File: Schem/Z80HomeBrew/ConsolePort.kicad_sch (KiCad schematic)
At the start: 12 parts, among them J3 0480370001, U14 FT230XS

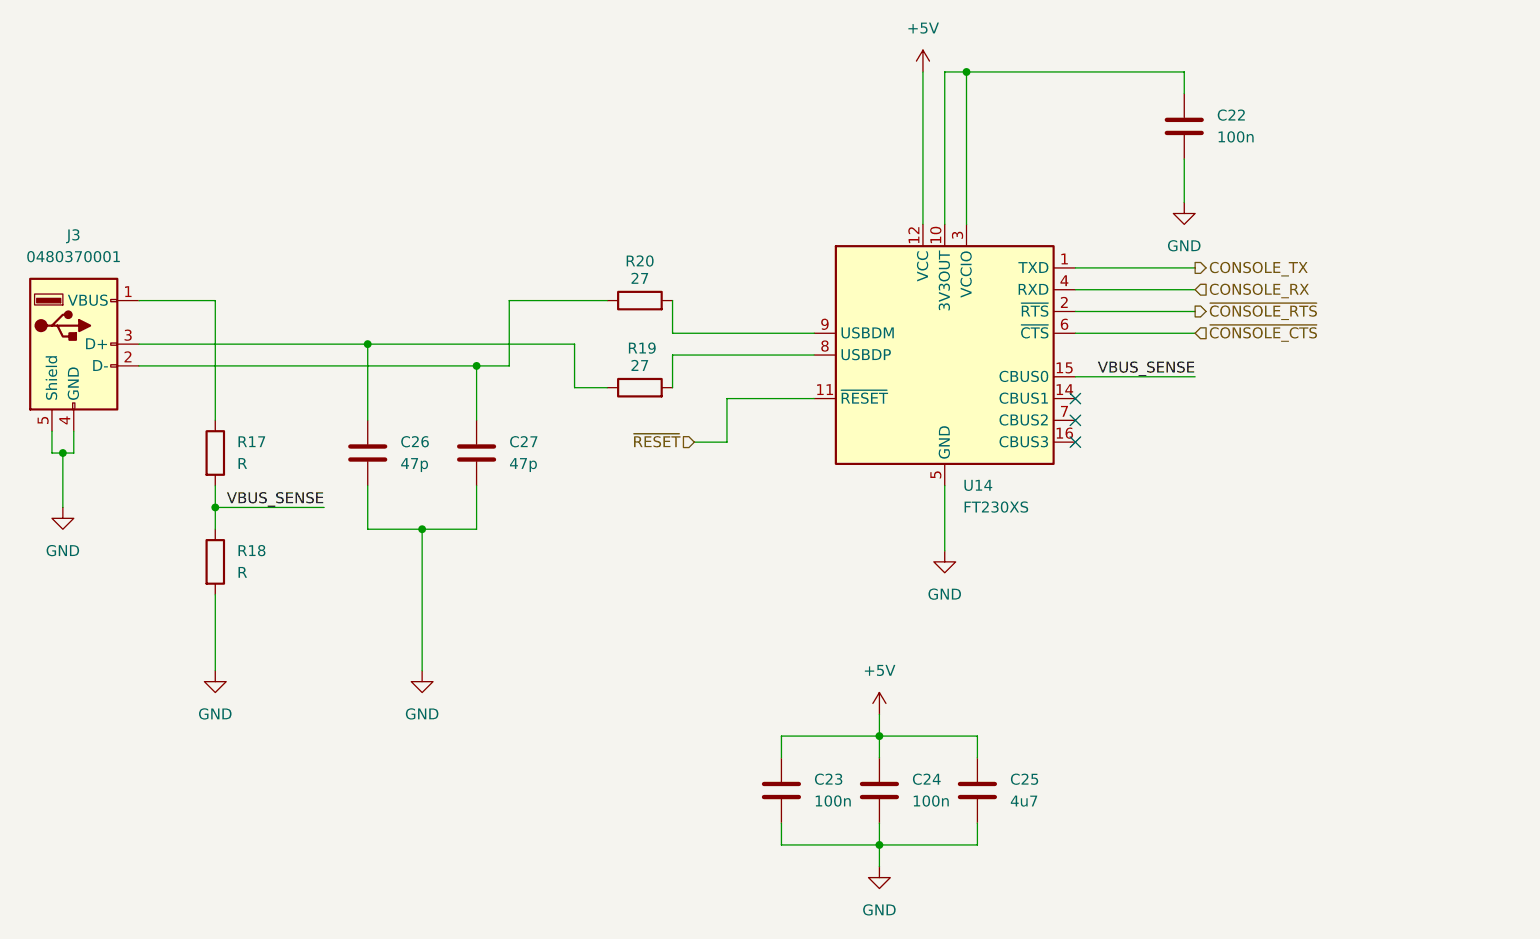
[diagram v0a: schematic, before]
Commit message: Video block added. fixed some issues with parts...
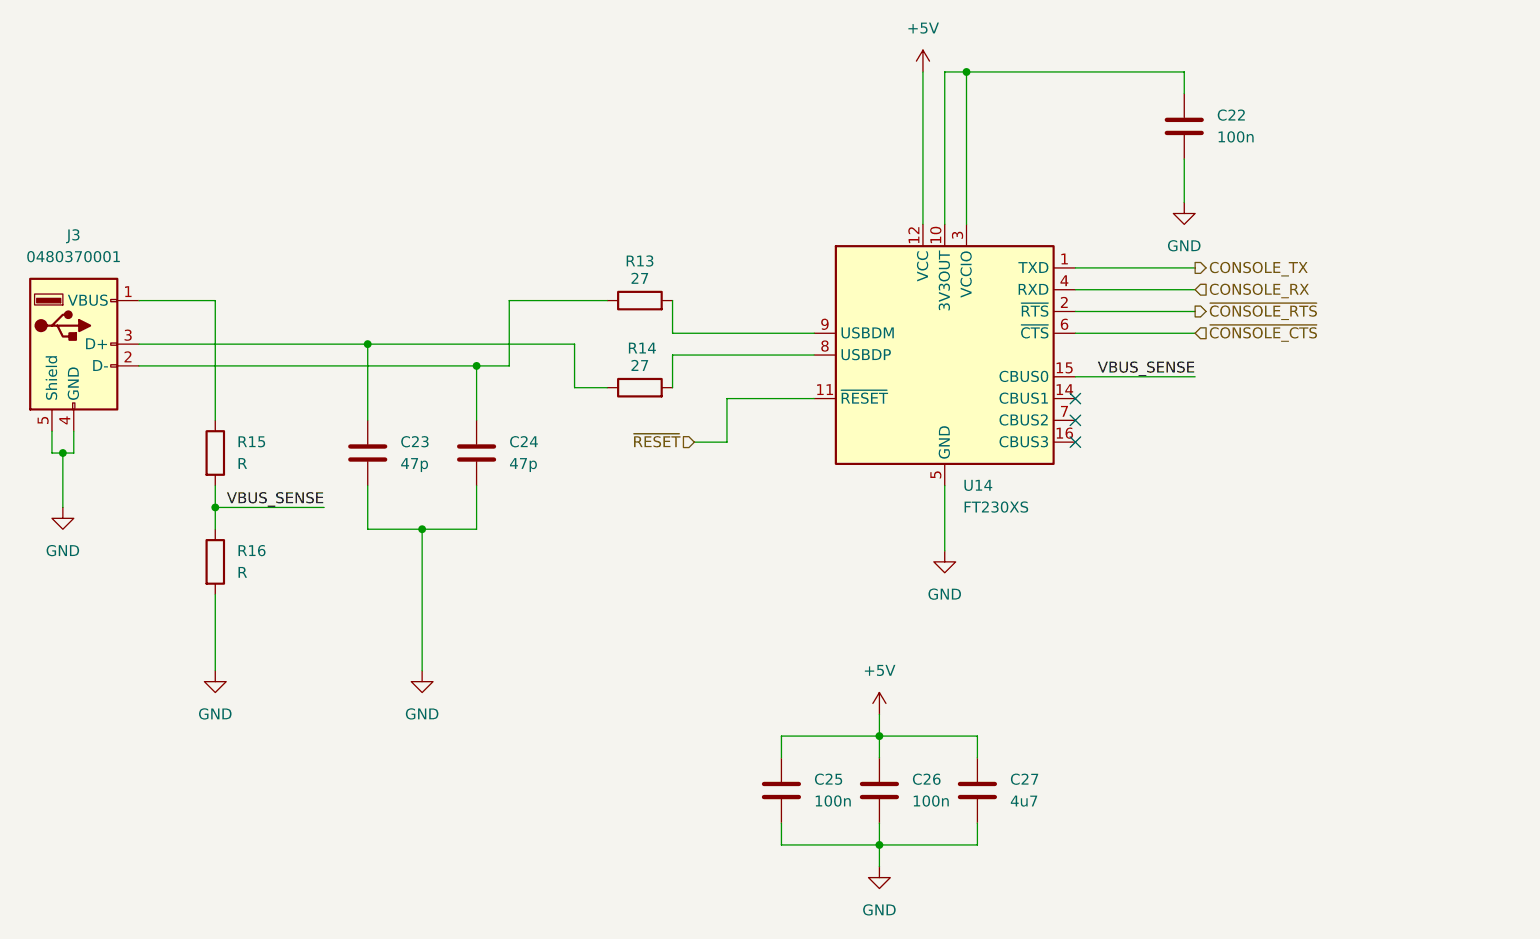
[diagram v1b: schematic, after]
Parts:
- renumbered C26 to C23, C27 to C24, C23 to C25, C24 to C26, C25 to C27, R20 to R13, R19 to R14, R17 to R15, R18 to R16
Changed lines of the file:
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@@
 		(dnp no)
 		(fields_autoplaced yes)
-		(property "Reference" "#PWR050"
+		(property "Reference" "#PWR054"
 			(at 153.67 38.1 0)
 			(effects
@@
 			(project ""
 				(path "/5593e793-d133-45d0-a91e-72805049e474/685e3ad0-b668-4082-bf36-08a728699034"
-					(reference "#PWR050")
+					(reference "#PWR054")
 					(unit 1)
 				)
@@
 		(dnp no)
 		(fields_autoplaced yes)
-		(property "Reference" "#PWR048"
+		(property "Reference" "#PWR055"
 			(at 184.15 55.88 0)
 			(effects
@@
 			(project ""
 				(path "/5593e793-d133-45d0-a91e-72805049e474/685e3ad0-b668-4082-bf36-08a728699034"
-					(reference "#PWR048")
+					(reference "#PWR055")
 					(unit 1)
 				)
@@
 		(dnp no)
 		(fields_autoplaced yes)
-		(property "Reference" "C24"
+		(property "Reference" "C26"
 			(at 152.4 116.8399 0)
 			(effects
@@
 			(project "Z80HomeBrew"
 				(path "/5593e793-d133-45d0-a91e-72805049e474/685e3ad0-b668-4082-bf36-08a728699034"
-					(reference "C24")
+					(reference "C26")
 					(unit 1)
 				)
@@
 		(on_board yes)
 		(dnp no)
-		(property "Reference" "R19"
+		(property "Reference" "R14"
 			(at 120.904 66.548 90)
 			(effects
@@
 			(project "Z80HomeBrew"
 				(path "/5593e793-d133-45d0-a91e-72805049e474/685e3ad0-b668-4082-bf36-08a728699034"
-					(reference "R19")
+					(reference "R14")
 					(unit 1)
 				)
@@
 		(on_board yes)
 		(dnp no)
-		(property "Reference" "R20"
+		(property "Reference" "R13"
 			(at 120.65 56.388 90)
 			(effects
@@
 			(project "Z80HomeBrew"
 				(path "/5593e793-d133-45d0-a91e-72805049e474/685e3ad0-b668-4082-bf36-08a728699034"
-					(reference "R20")
+					(reference "R13")
 					(unit 1)
 				)
@@
 		(dnp no)
 		(fields_autoplaced yes)
-		(property "Reference" "#PWR051"
+		(property "Reference" "#PWR060"
 			(at 148.59 113.03 0)
 			(effects
@@
 			(project "Z80HomeBrew"
 				(path "/5593e793-d133-45d0-a91e-72805049e474/685e3ad0-b668-4082-bf36-08a728699034"
-					(reference "#PWR051")
+					(reference "#PWR060")
 					(unit 1)
 				)
@@
 		(dnp no)
 		(fields_autoplaced yes)
-		(property "Reference" "#PWR049"
+		(property "Reference" "#PWR057"
 			(at 156.21 96.52 0)
 			(effects
@@
 			(project "Z80HomeBrew"
 				(path "/5593e793-d133-45d0-a91e-72805049e474/685e3ad0-b668-4082-bf36-08a728699034"
-					(reference "#PWR049")
+					(reference "#PWR057")
 					(unit 1)
 				)
@@
 		(dnp no)
 		(fields_autoplaced yes)
-		(property "Reference" "#PWR052"
+		(property "Reference" "#PWR061"
 			(at 148.59 133.35 0)
 			(effects
@@
 			(project "Z80HomeBrew"
 				(path "/5593e793-d133-45d0-a91e-72805049e474/685e3ad0-b668-4082-bf36-08a728699034"
-					(reference "#PWR052")
+					(reference "#PWR061")
 					(unit 1)
 				)
@@
 		(dnp no)
 		(fields_autoplaced yes)
-		(property "Reference" "C25"
+		(property "Reference" "C27"
 			(at 163.83 116.8399 0)
 			(effects
@@
 			(project "Z80HomeBrew"
 				(path "/5593e793-d133-45d0-a91e-72805049e474/685e3ad0-b668-4082-bf36-08a728699034"
-					(reference "C25")
+					(reference "C27")
 					(unit 1)
 				)
@@
 		(dnp no)
 		(fields_autoplaced yes)
-		(property "Reference" "C23"
+		(property "Reference" "C25"
 			(at 140.97 116.8399 0)
 			(effects
@@
 			(project "Z80HomeBrew"
 				(path "/5593e793-d133-45d0-a91e-72805049e474/685e3ad0-b668-4082-bf36-08a728699034"
-					(reference "C23")
+					(reference "C25")
 					(unit 1)
 				)
@@
 		(dnp no)
 		(fields_autoplaced yes)
-		(property "Reference" "R17"
+		(property "Reference" "R15"
 			(at 73.66 77.4699 0)
 			(effects
@@
 			(project ""
 				(path "/5593e793-d133-45d0-a91e-72805049e474/685e3ad0-b668-4082-bf36-08a728699034"
-					(reference "R17")
+					(reference "R15")
 					(unit 1)
 				)
@@
 		(dnp no)
 		(fields_autoplaced yes)
-		(property "Reference" "C26"
+		(property "Reference" "C23"
 			(at 92.71 77.4699 0)
 			(effects
@@
 			(project "Z80HomeBrew"
 				(path "/5593e793-d133-45d0-a91e-72805049e474/685e3ad0-b668-4082-bf36-08a728699034"
-					(reference "C26")
+					(reference "C23")
 					(unit 1)
 				)
@@
 		(dnp no)
 		(fields_autoplaced yes)
-		(property "Reference" "C27"
+		(property "Reference" "C24"
 			(at 105.41 77.4699 0)
 			(effects
@@
 			(project "Z80HomeBrew"
 				(path "/5593e793-d133-45d0-a91e-72805049e474/685e3ad0-b668-4082-bf36-08a728699034"
-					(reference "C27")
+					(reference "C24")
 					(unit 1)
 				)
@@
 		(dnp no)
 		(fields_autoplaced yes)
-		(property "Reference" "#PWR054"
+		(property "Reference" "#PWR059"
 			(at 95.25 110.49 0)
 			(effects
@@
 			(project "Z80HomeBrew"
 				(path "/5593e793-d133-45d0-a91e-72805049e474/685e3ad0-b668-4082-bf36-08a728699034"
-					(reference "#PWR054")
+					(reference "#PWR059")
 					(unit 1)
 				)
@@
 		(dnp no)
 		(fields_autoplaced yes)
-		(property "Reference" "#PWR055"
+		(property "Reference" "#PWR056"
 			(at 53.34 91.44 0)
 			(effects
@@
 			(project "Z80HomeBrew"
 				(path "/5593e793-d133-45d0-a91e-72805049e474/685e3ad0-b668-4082-bf36-08a728699034"
-					(reference "#PWR055")
+					(reference "#PWR056")
 					(unit 1)
 				)
@@
 		(dnp no)
 		(fields_autoplaced yes)
-		(property "Reference" "#PWR053"
+		(property "Reference" "#PWR058"
 			(at 71.12 110.49 0)
 			(effects
@@
 			(project "Z80HomeBrew"
 				(path "/5593e793-d133-45d0-a91e-72805049e474/685e3ad0-b668-4082-bf36-08a728699034"
-					(reference "#PWR053")
+					(reference "#PWR058")
 					(unit 1)
 				)
@@
 		(dnp no)
 		(fields_autoplaced yes)
-		(property "Reference" "R18"
+		(property "Reference" "R16"
 			(at 73.66 90.1699 0)
 			(effects
@@
 			(project "Z80HomeBrew"
 				(path "/5593e793-d133-45d0-a91e-72805049e474/685e3ad0-b668-4082-bf36-08a728699034"
-					(reference "R18")
-					(unit 1)
-				)
+					(reference "R16")
+					(unit 1)
+				)

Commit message: Completed schematics
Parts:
- U14: value FT230XS -> FT230XS-U
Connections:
- net VBUS_SENSE: no longer U14.15 (CBUS0)
- net ~{CONSOLE_CTS} renamed CONSOLE_CTS
- net ~{CONSOLE_RTS} renamed CONSOLE_RTS
- new net CONSOLE_DTR: U14.15 (CBUS0)
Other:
- note added: "Configure the FT230 so that CBUS0 (PWREN#) is asserted (low) to signal that a terminal is connected (DTR)"
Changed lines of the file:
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@@
 	(generator_version "9.0")
 	(paper "USLedger")
+	(text "Configure the FT230 so that \nCBUS0 (PWREN#) is asserted \n(low) to signal that a terminal\nis connected (DTR)"
+		(exclude_from_sim no)
+		(at 173.482 75.438 0)
+		(effects
+			(font
+				(size 1.27 1.27)
+			)
+			(justify left)
+		)
+	)
 	(junction
 		(at 148.59 124.46)
@@
 		(color 0 0 0 0)
 	)
+	(junction
+		(at 67.31 60.96)
+		(diameter 0)
+		(color 0 0 0 0)
+	)
 	(no_connect
 		(at 171.45 72.39)
@@
 	(wire
 		(pts
-			(xy 62.23 60.96) (xy 71.12 60.96)
+			(xy 62.23 60.96) (xy 67.31 60.96)
 		)
 		(stroke
@@
 		(pts
 			(xy 124.46 71.12) (xy 124.46 67.31)
+		)
+		(stroke
+			(width 0)
+			(type default)
+		)
+	)
+	(wire
+		(pts
+			(xy 67.31 60.96) (xy 71.12 60.96)
 		)
 		(stroke
@@
 		)
 	)
-	(label "VBUS_SENSE"
-		(at 185.42 69.85 180)
+	(hierarchical_label "CONSOLE_RTS"
+		(shape output)
+		(at 185.42 62.23 0)
 		(effects
 			(font
 				(size 1.27 1.27)
 			)
-			(justify right bottom)
-		)
-	)
-	(hierarchical_label "~{CONSOLE_RTS}"
+			(justify left)
+		)
+	)
+	(hierarchical_label "CONSOLE_DTR"
 		(shape output)
-		(at 185.42 62.23 0)
+		(at 185.42 69.85 0)
 		(effects
 			(font
@@
 		)
 	)
-	(hierarchical_label "~{CONSOLE_CTS}"
+	(hierarchical_label "CONSOLE_CTS"
 		(shape input)
 		(at 185.42 64.77 0)
@@
 			)
 		)
-		(property "Value" "FT230XS"
+		(property "Value" "FT230XS-U"
 			(at 158.3533 85.09 0)
 			(effects
@@
 					(unit 1)
 				)
+			)
+		)
+	)
+	(symbol
+		(lib_id "power:PWR_FLAG")
+		(at 67.31 60.96 0)
+		(unit 1)
+		(exclude_from_sim no)
+		(in_bom yes)
+		(on_board yes)
+		(dnp no)
+		(fields_autoplaced yes)
+		(property "Reference" "#FLG05"
+			(at 67.31 59.055 0)
+			(effects
+				(font
+					(size 1.27 1.27)
+				)
+				(hide yes)
+			)
+		)
+		(property "Value" "PWR_FLAG"
+			(at 67.31 55.88 0)
+			(effects
+				(font
+					(size 1.27 1.27)
+				)
+			)
+		)
+		(property "Footprint" ""
+			(at 67.31 60.96 0)
+			(effects
+				(font
+					(size 1.27 1.27)
+				)
+				(hide yes)
+			)
+		)
+		(property "Datasheet" "~"
+			(at 67.31 60.96 0)
+			(effects
+				(font
+					(size 1.27 1.27)
+				)
+				(hide yes)
+			)
+		)
+		(property "Description" "Special symbol for telling ERC where power comes from"
+			(at 67.31 60.96 0)
+			(effects
+				(font
+					(size 1.27 1.27)
+				)
+				(hide yes)
+			)
+		)
+		(pin "1"
+		)
+		(instances
+			(project ""
+				(path "/5593e793-d133-45d0-a91e-72805049e474/685e3ad0-b668-4082-bf36-08a728699034"
+					(reference "#FLG05")
+					(unit 1)
+				)

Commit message: Finally found a name "Zephyr-80" for the brew and committing the first pbc
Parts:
- removed C25: 100n, Capacitor_SMD:C_0603_1608Metric, symbol Device:C
- added J16: Conn_01x04, Connector_PinSocket_2.54mm:PinSocket_1x04_P2.54mm_Vertical, symbol Connector_Generic:Conn_01x04
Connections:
- net GND: now also J16.3 (Pin_3)
- net VBUS_SENSE: now also U14.14 (CBUS1)
- net VBUS_PIN1: now reaches J3.1 (VBUS), R15.1
- net VBUS_PIN1: now also J16.1 (Pin_1)
- net DM1: now reaches C24.1, J3.2 (D-), R13.1
- net DM1: now also J16.2 (Pin_2)
- net DP1: now reaches C23.1, J3.3 (D+), R14.1
- net DP1: now also J16.4 (Pin_4)
- no-connect marks 3 -> 2
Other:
- note added: "Alternative header for USB Console"
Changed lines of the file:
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@@
 	(generator_version "9.0")
 	(paper "USLedger")
+	(text "Alternative header\nfor USB Console"
+		(exclude_from_sim no)
+		(at 70.866 46.228 0)
+		(effects
+			(font
+				(size 1.27 1.27)
+			)
+		)
+	)
 	(text "Configure the FT230 so that \nCBUS0 (PWREN#) is asserted \n(low) to signal that a terminal\nis connected (DTR)"
 		(exclude_from_sim no)
-		(at 173.482 75.438 0)
+		(at 185.42 75.184 0)
 		(effects
 			(font
@@
 	)
 	(junction
+		(at 71.12 63.5)
+		(diameter 0)
+		(color 0 0 0 0)
+	)
+	(junction
 		(at 101.6 68.58)
 		(diameter 0)
@@
 	)
 	(no_connect
-		(at 171.45 72.39)
-	)
-	(no_connect
 		(at 171.45 77.47)
 	)
@@
 	(wire
 		(pts
-			(xy 71.12 60.96) (xy 71.12 74.93)
+			(xy 71.12 60.96) (xy 71.12 63.5)
 		)
 		(stroke
@@
 	(wire
 		(pts
-			(xy 137.16 111.76) (xy 148.59 111.76)
+			(xy 83.82 39.37) (xy 83.82 49.53)
 		)
 		(stroke
@@
 	(wire
 		(pts
-			(xy 137.16 121.92) (xy 137.16 124.46)
-		)
-		(stroke
-			(width 0)
-			(type default)
-		)
-	)
-	(wire
-		(pts
 			(xy 95.25 87.63) (xy 95.25 104.14)
 		)
@@
 	(wire
 		(pts
+			(xy 74.93 39.37) (xy 83.82 39.37)
+		)
+		(stroke
+			(width 0)
+			(type default)
+		)
+	)
+	(wire
+		(pts
 			(xy 88.9 66.04) (xy 88.9 74.93)
 		)
@@
 	(wire
 		(pts
+			(xy 74.93 36.83) (xy 78.74 36.83)
+		)
+		(stroke
+			(width 0)
+			(type default)
+		)
+	)
+	(wire
+		(pts
+			(xy 85.09 34.29) (xy 74.93 34.29)
+		)
+		(stroke
+			(width 0)
+			(type default)
+		)
+	)
+	(wire
+		(pts
 			(xy 148.59 124.46) (xy 160.02 124.46)
 		)
@@
 	(wire
 		(pts
-			(xy 137.16 114.3) (xy 137.16 111.76)
+			(xy 71.12 63.5) (xy 82.55 63.5)
 		)
 		(stroke
@@
 	(wire
 		(pts
+			(xy 80.01 41.91) (xy 74.93 41.91)
+		)
+		(stroke
+			(width 0)
+			(type default)
+		)
+	)
+	(wire
+		(pts
 			(xy 54.61 78.74) (xy 53.34 78.74)
 		)
@@
 	(wire
 		(pts
-			(xy 137.16 124.46) (xy 148.59 124.46)
+			(xy 171.45 72.39) (xy 185.42 72.39)
 		)
 		(stroke
@@
 	(wire
 		(pts
+			(xy 71.12 63.5) (xy 71.12 74.93)
+		)
+		(stroke
+			(width 0)
+			(type default)
+		)
+	)
+	(wire
+		(pts
 			(xy 158.75 34.29) (xy 158.75 52.07)
 		)
@@
 			(width 0)
 			(type default)
+		)
+	)
+	(label "DP1"
+		(at 80.01 41.91 180)
+		(effects
+			(font
+				(size 1.27 1.27)
+			)
+			(justify right bottom)
+		)
+	)
+	(label "VBUS_SENSE"
+		(at 185.42 72.39 180)
+		(effects
+			(font
+				(size 1.27 1.27)
+			)
+			(justify right bottom)
 		)
 	)
 	(label "VBUS_SENSE"
 		(at 83.82 85.09 180)
+		(effects
+			(font
+				(size 1.27 1.27)
+			)
+			(justify right bottom)
+		)
+	)
+	(label "VBUS_PIN1"
+		(at 85.09 34.29 180)
+		(effects
+			(font
+				(size 1.27 1.27)
+			)
+			(justify right bottom)
+		)
+	)
+	(label "DM1"
+		(at 68.58 68.58 180)
+		(effects
+			(font
+				(size 1.27 1.27)
+			)
+			(justify right bottom)
+		)
+	)
+	(label "DM1"
+		(at 78.74 36.83 180)
+		(effects
+			(font
+				(size 1.27 1.27)
+			)
+			(justify right bottom)
+		)
+	)
+	(label "DP1"
+		(at 68.58 66.04 180)
+		(effects
+			(font
+				(size 1.27 1.27)
+			)
+			(justify right bottom)
+		)
+	)
+	(label "VBUS_PIN1"
+		(at 82.55 63.5 180)
 		(effects
 			(font
@@
 	)
 	(symbol
+		(lib_id "Connector_Generic:Conn_01x04")
+		(at 69.85 36.83 0)
+		(mirror y)
+		(unit 1)
+		(exclude_from_sim no)
+		(in_bom yes)
+		(on_board yes)
+		(dnp no)
+		(fields_autoplaced yes)
+		(property "Reference" "J16"
+			(at 67.31 36.8299 0)
+			(effects
+				(font
+					(size 1.27 1.27)
+				)
+				(justify left)
+			)
+		)
+		(property "Value" "Conn_01x04"
+			(at 67.31 39.3699 0)
+			(effects
+				(font
+					(size 1.27 1.27)
+				)
+				(justify left)
+			)
+		)
+		(property "Footprint" "Connector_PinSocket_2.54mm:PinSocket_1x04_P2.54mm_Vertical"
+			(at 69.85 36.83 0)
+			(effects
+				(font
+					(size 1.27 1.27)
+				)
+				(hide yes)
+			)
+		)
+		(property "Datasheet" "~"
+			(at 69.85 36.83 0)
+			(effects
+				(font
+					(size 1.27 1.27)
+				)
+				(hide yes)
+			)
+		)
+		(property "Description" "Generic connector, single row, 01x04, script generated (kicad-library-utils/schlib/autogen/connector/)"
+			(at 69.85 36.83 0)
+			(effects
+				(font
+					(size 1.27 1.27)
+				)
+				(hide yes)
+			)
+		)
+		(pin "2"
+		)
+		(pin "4"
+		)
+		(pin "3"
+		)
+		(pin "1"
+		)
+		(instances
+			(project "Z80HomeBrew"
+				(path "/5593e793-d133-45d0-a91e-72805049e474/685e3ad0-b668-4082-bf36-08a728699034"
+					(reference "J16")
+					(unit 1)
+				)
+			)
+		)
+	)
+	(symbol
 		(lib_id "Device:C")
 		(at 148.59 118.11 0)
@@
 	)
 	(symbol
-		(lib_id "Device:C")
-		(at 137.16 118.11 0)
-		(unit 1)
-		(exclude_from_sim no)
-		(in_bom yes)
-		(on_board yes)
-		(dnp no)
-		(fields_autoplaced yes)
-		(property "Reference" "C25"
-			(at 140.97 116.8399 0)
-			(effects
-				(font
-					(size 1.27 1.27)
-				)
-				(justify left)
-			)
-		)
-		(property "Value" "100n"
-			(at 140.97 119.3799 0)
-			(effects
-				(font
-					(size 1.27 1.27)
-				)
-				(justify left)
-			)
-		)
-		(property "Footprint" "Capacitor_SMD:C_0603_1608Metric"
-			(at 138.1252 121.92 0)
-			(effects
-				(font
-					(size 1.27 1.27)
-				)
-				(hide yes)
-			)
-		)
-		(property "Datasheet" "~"
-			(at 137.16 118.11 0)
-			(effects
-				(font
-					(size 1.27 1.27)
-				)
-				(hide yes)
-			)
-		)
-		(property "Description" "Unpolarized capacitor"
-			(at 137.16 118.11 0)
-			(effects
-				(font
-					(size 1.27 1.27)
-				)
-				(hide yes)
-			)
-		)
-		(pin "1"
-		)
-		(pin "2"
-		)
-		(instances
-			(project "Z80HomeBrew"
-				(path "/5593e793-d133-45d0-a91e-72805049e474/685e3ad0-b668-4082-bf36-08a728699034"
-					(reference "C25")
-					(unit 1)
-				)
-			)
-		)
-	)
-	(symbol
 		(lib_id "Device:R")
 		(at 71.12 78.74 0)
@@
 					(unit 1)
 				)
+			)
+		)
+	)
+	(symbol
+		(lib_id "power:GND")
+		(at 83.82 49.53 0)
+		(unit 1)
+		(exclude_from_sim no)
+		(in_bom yes)
+		(on_board yes)
+		(dnp no)
+		(fields_autoplaced yes)
+		(property "Reference" "#PWR0147"
+			(at 83.82 55.88 0)
+			(effects
+				(font
+					(size 1.27 1.27)
+				)
+				(hide yes)
+			)
+		)
+		(property "Value" "GND"
+			(at 83.82 54.61 0)
+			(effects
+				(font
+					(size 1.27 1.27)
+				)
+			)
+		)
+		(property "Footprint" ""
+			(at 83.82 49.53 0)
+			(effects
+				(font
+					(size 1.27 1.27)
+				)
+				(hide yes)
+			)
+		)
+		(property "Datasheet" ""
+			(at 83.82 49.53 0)
+			(effects
+				(font
+					(size 1.27 1.27)
+				)
+				(hide yes)
+			)
+		)
+		(property "Description" "Power symbol creates a global label with name \"GND\" , ground"
+			(at 83.82 49.53 0)
+			(effects
+				(font
+					(size 1.27 1.27)
+				)
+				(hide yes)
+			)
+		)
+		(pin "1"
+		)
+		(instances
+			(project "Z80HomeBrew"
+				(path "/5593e793-d133-45d0-a91e-72805049e474/685e3ad0-b668-4082-bf36-08a728699034"
+					(reference "#PWR0147")
+					(unit 1)
+				)
